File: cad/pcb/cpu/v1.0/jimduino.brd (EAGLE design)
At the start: 38 x 31 mm, 37 parts, among them P1 DF12-32-DP, P2 DF12-32-DP, Q1 FDN360P, SW1 ON/OFF, U1 STM32F415R, U2 MCP1703, U4 LTC2954-2, Y1 8Y-16.000MAAV-T, Y2 16MHz

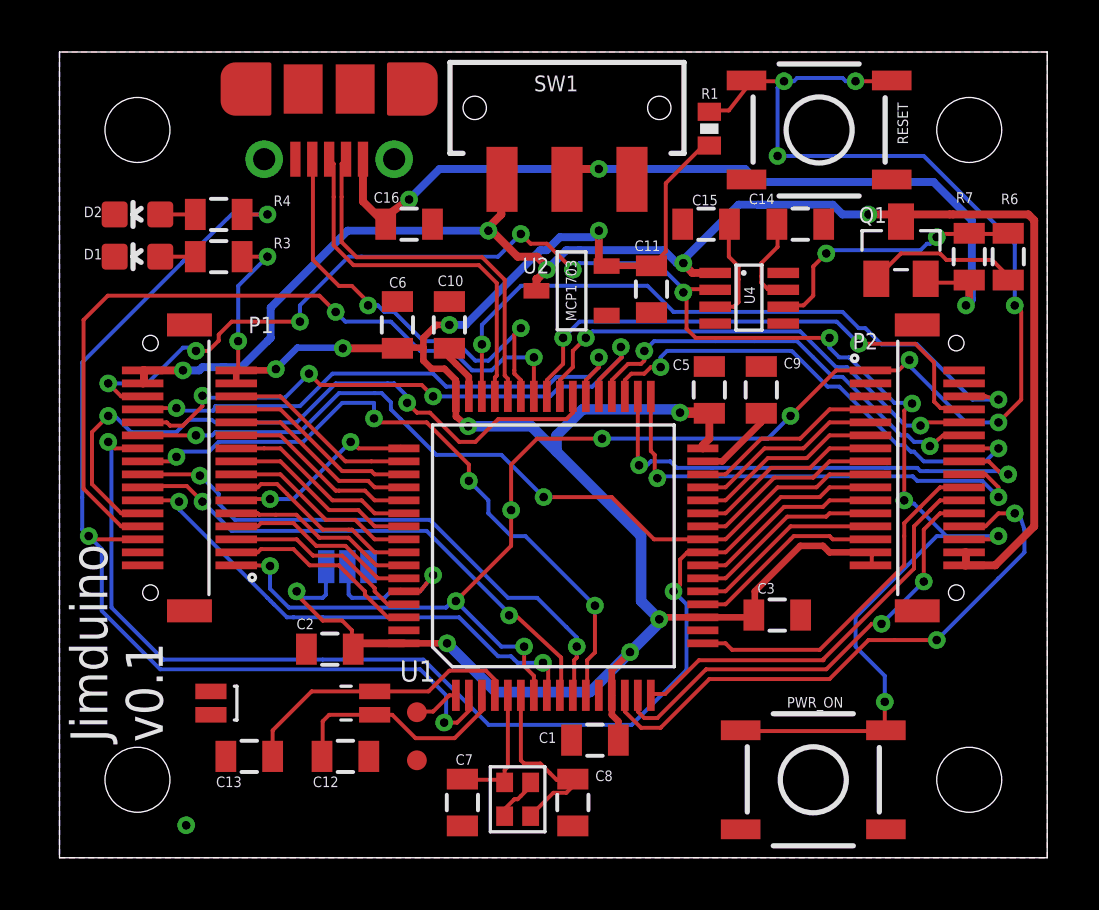
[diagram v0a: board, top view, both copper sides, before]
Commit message: Move components and switches around.
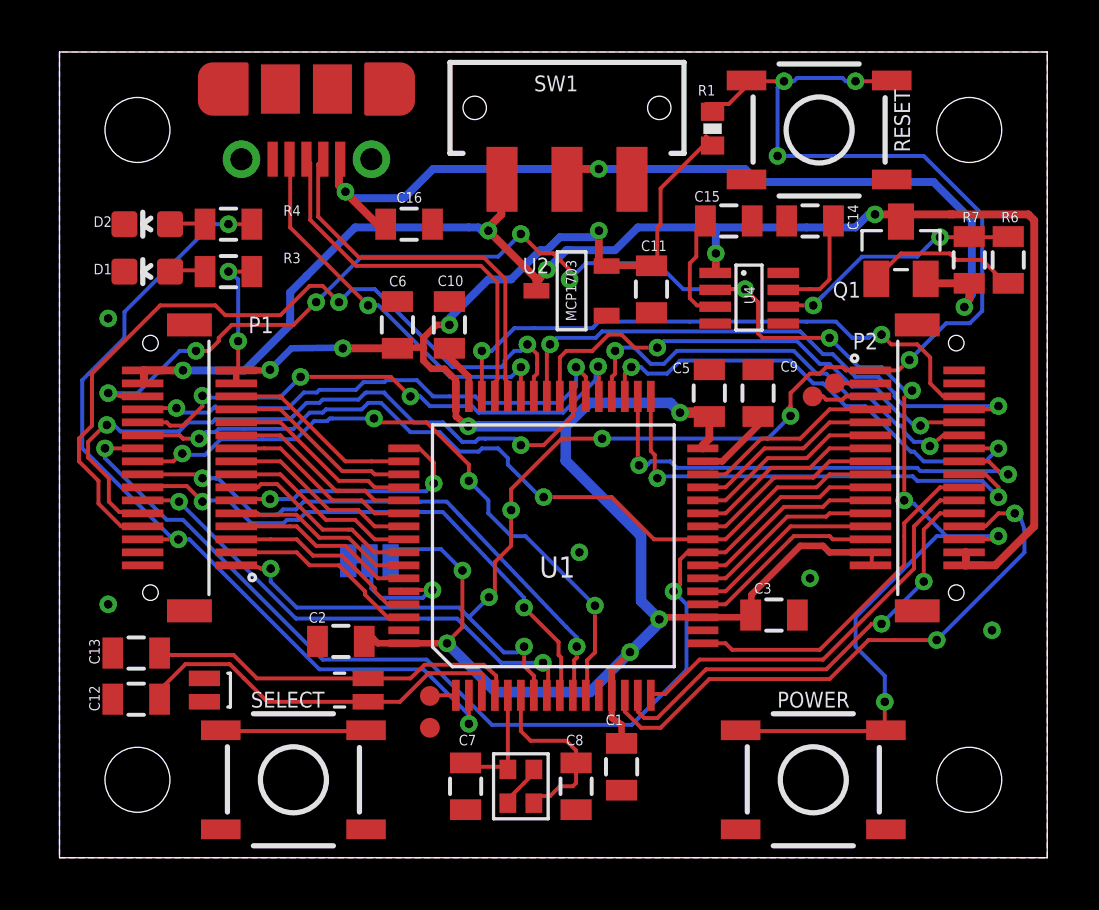
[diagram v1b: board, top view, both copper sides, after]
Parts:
- added SELECT: SWITCH-MOMENTARY-2SMD-REDUNDANT, SparkFun-Electromechanical:TACTILE-SWITCH-SMD
- added TP3, TP4: TEST-POINT3, SparkFun-Passives:PAD.03X.03
- C15: value 0.033uF -> .033uF
- moved C12 8.35 mm to (2.95, 6.10), turned to 180 degrees
- moved C13 5.89 mm to (2.95, 7.88)
- moved C1 1.45 mm to (21.6, 3.50), turned to 270 degrees
- moved TP2 1.35 mm to (14.2, 5.00)
- moved C15 0.88 mm to (25.8, 24.5), turned to 0 degrees
- moved BOOT0 0.88 mm to (11.9, 11.4), turned to 0 degrees
- moved U$3 0.88 mm to (12.0, 26.9)
- moved TP1 0.80 mm to (14.2, 6.22)
- moved D1 0.69 mm to (3.38, 22.6)
- moved R3 0.69 mm to (6.50, 22.6)
- moved C7 0.64 mm to (15.6, 2.75)
- moved C8 0.64 mm to (19.9, 2.75)
- moved Y2 0.56 mm to (12.5, 7.20)
- moved D2 0.53 mm to (3.38, 24.4)
- moved R4 0.53 mm to (6.50, 24.4)
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- renumbered PWR_ON to POWER
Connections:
- new net RSV0: P2.3, TP3.P$1
- new net RSV1: P2.5, TP4.P$1
- new net SELECT: SELECT.1, SELECT.2
- net GND: now also SELECT.3, SELECT.4
- net VCC_SW: no longer U4.1
- net VCC_USB: now also U4.1
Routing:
- net PC13: track 40.2 -> 34.3 mm
- net RESET#: track 74.8 -> 69.0 mm, vias 12 -> 10
- net SELECT: track 0.00 -> 5.61 mm
- net OSC32K_IN: track 10.0 -> 15.1 mm
- net PA13: track 26.5 -> 22.7 mm
- net PC4: track 45.8 -> 42.4 mm
- net OSC32K_OUT: track 11.3 -> 14.6 mm
- net PA14: track 7.60 -> 10.4 mm
- net RSV1: track 0.00 -> 2.33 mm
- net PC6: track 23.3 -> 21.5 mm
- net USB_ID: track 16.9 -> 15.2 mm
- net PA8: track 20.5 -> 22.1 mm
- net VCC_USB: track 36.5 -> 38.0 mm
- net BOOT0: track 6.52 -> 5.11 mm
- net RSV0: track 0.00 -> 1.37 mm
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
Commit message: Add LIPO charging circuit.
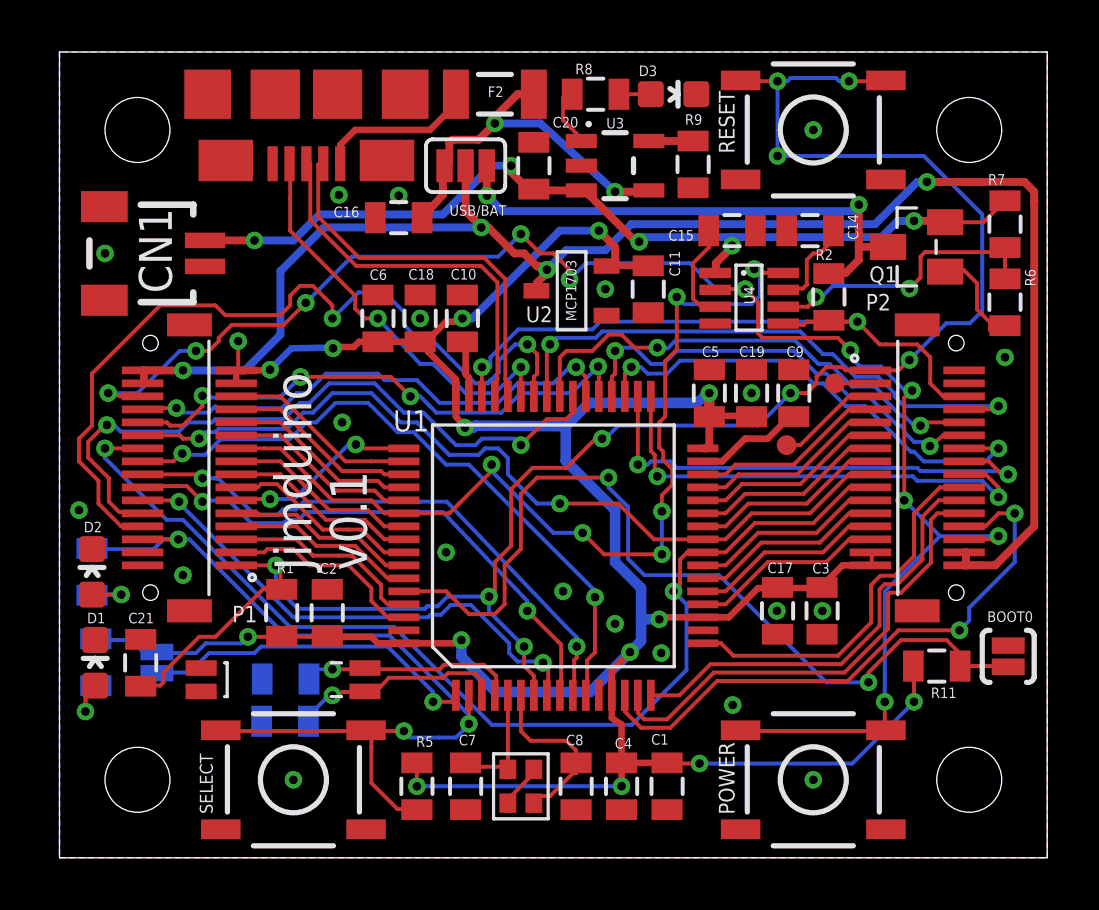
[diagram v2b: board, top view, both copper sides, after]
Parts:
- removed SW1: ON/OFF, SparkFun-Electromechanical:SWITCH-SPDT-SMD
- removed TP1, TP2: TEST-POINT3, SparkFun-Passives:PAD.03X.03
- removed U$3: USB-CON-5PIN-105017-0001, GeekAmmo:USB-MICRO-MOLEX-105017-0001
- added BKUP: JUMPER-PAD-2-NC_BY_PASTE, SparkFun-Passives:PAD-JUMPER-2-NC_BY_PASTE_YES_SILK
- added C17, C18, C21, C4: 0.1uF, SparkFun-Capacitors:0805
- added C19: 1uF, SparkFun-Capacitors:0805
- added C20: 10uF, SparkFun-Capacitors:0805
- added CN1: SM02B-SRSS-TB, con-jst2:SM02B-SRSS-TB
- added D3: CHG, SparkFun-LED:LED-0603
- added F2: PTCSMD, SparkFun-PowerIC:PTC-1206
- added P3: MICROUSB, jimduino:MICROUSB
- added R11, R2, R5: 10k, SparkFun-Passives:0805
- added R8: 1k, SparkFun-Passives:0805
- added R9: 4.7k, SparkFun-Passives:0805
- added U3: MCP73831, SparkFun-PowerIC:SOT23-5
- added USB/BAT: JUMPER-PAD-3-2OF3_NC_BY_PASTE, SparkFun-Passives:PAD-JUMPER-3-2OF3_NC_BY_PASTE_YES_SILK_FULL_BOX
- BOOT0: value JUMPER-PAD-3-2OF3_NC_BY_PASTE -> JUMPER-PAD-2-NC_BY_PASTE; device SparkFun-Passives:PAD-JUMPER-3-2OF3_NC_BY_PASTE_YES_SILK_FULL_BOX -> SparkFun-Passives:PAD-JUMPER-2-NC_BY_PASTE_YES_SILK
- C5: value 1uF -> 0.1uF
- D1: value RED_PWR -> PWR
- D2: value GREEN_PC13 -> PC13
- R1: device SparkFun-Passives:0402-RES -> SparkFun-Passives:0805
- R3, R4: value 270 -> 1k
- Y2: value 16MHz -> 32.768kHz
- moved R1 24.9 mm to (8.55, 9.43)
- moved BOOT0 24.8 mm to (36.5, 7.75), flipped to the top, turned to 90 degrees
- moved R3 15.9 mm to (1.40, 7.53), flipped to the bottom, turned to 90 degrees
- moved D1 15.2 mm to (1.38, 7.50), turned to 0 degrees
- moved R4 14.4 mm to (1.25, 11.0), flipped to the bottom, turned to 90 degrees
- moved D2 13.5 mm to (1.25, 11.0), turned to 0 degrees
- moved C13 5.84 mm to (8.70, 6.88), flipped to the bottom, turned to 0 degrees
- moved C12 5.79 mm to (8.68, 5.25), flipped to the bottom, turned to 0 degrees
- moved TP4 2.12 mm to (28.0, 15.9)
- moved R7 1.94 mm to (36.4, 24.4), turned to 270 degrees
- moved C1 1.90 mm to (23.4, 2.75)
- moved C3 1.86 mm to (29.3, 9.50), turned to 270 degrees
- moved R6 1.63 mm to (36.4, 21.4)
- moved C9 1.38 mm to (28.2, 17.9)
- moved C2 1.22 mm to (10.3, 9.43), turned to 90 degrees
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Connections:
- removed net INT#: U4.5
- removed net KILL#: U4.8
- removed net SELECT: SELECT.1, SELECT.2
- removed net USB_ID: U$3.4, U1.43
- removed net USB_N: U$3.2, U1.44
- removed net USB_P: U$3.3, U1.45
- removed net VCC_SW: P1.30, P1.32, P2.30, P2.32, Q1.3, SW1.1, U2.3
- new net N$10: D3.A, R8.1
- new net N$11: R9.1, U3.5
- new net PA10: P3.P$4, U1.43
- new net PA11: P3.P$2, U1.44
- new net PA12: P3.P$3, U1.45
- new net STAT: R8.2, U3.1
- new net VCC: P1.30, P1.32, P2.30, P2.32, U2.3, USB/BAT.2
- new net VCC_BKUP: BKUP.1, U1.1
- new net VCC_SOFT: Q1.3, R2.1, USB/BAT.1
- new net VCC_USB_FUSED: C16.1, F2.2, U3.4, USB/BAT.3
- net BOOT0: now also BOOT0.1, R11.1; no longer BOOT0.2
- net GND: now also BOOT0.2, C17.2, C18.2, C19.2, C20.2, C21.2, C4.2, CN1.2, D3.C, P3.P$5, R9.2, U3.2; no longer BOOT0.3, TP2.P$1, U$3.5
- net PA13: now also R2.2, U4.5
- net PC13: now also R5.1, SELECT.1, SELECT.2
- net PD2: now also U4.8
- net RESET#: now also C21.1
- net VBAT: now also C20.1, CN1.1, Q1.2, R7.1, U3.3, U4.1; no longer TP1.P$1, U1.1
- net VCC_3V3: now also BKUP.2, C17.1, C18.1, C19.1, C4.1, R11.2, R5.2; no longer BOOT0.1
- net VCC_USB: now also F2.1, P3.P$1; no longer C16.1, Q1.2, R7.1, SW1.2, U$3.1, U4.1
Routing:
- net VCC: track 0.00 -> 61.8 mm, vias 0 -> 4
- net VCC_SW: track 60.6 -> 0.00 mm, vias 5 -> 0
- net VBAT: track 1.00 -> 36.5 mm, vias 0 -> 5
- net VCC_USB: track 38.0 -> 6.63 mm, vias 3 -> 0
- net BOOT0: track 5.11 -> 34.6 mm, vias 1 -> 2
- net PD2: track 7.49 -> 36.6 mm, vias 0 -> 6
- net VCC_3V3: track 92.4 -> 113.3 mm, vias 12 -> 15
- net VCC_SOFT: track 0.00 -> 20.4 mm, vias 0 -> 2
- net PA10: track 0.00 -> 16.5 mm, vias 0 -> 2
- net USB_ID: track 15.2 -> 0.00 mm, vias 2 -> 0
- net USB_N: track 15.0 -> 0.00 mm
- net USB_P: track 15.0 -> 0.00 mm
- net PA12: track 0.00 -> 15.0 mm
- net PA11: track 0.00 -> 15.0 mm
- net VCC_USB_FUSED: track 0.00 -> 14.4 mm, vias 0 -> 2
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
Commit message: Add more intelligent power switching and improve schematic layout.
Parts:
- removed F2: PTCSMD, SparkFun-PowerIC:PTC-1206
- removed TP4: TEST-POINT3, SparkFun-Passives:PAD.03X.03
- removed USB/BAT: JUMPER-PAD-3-2OF3_NC_BY_PASTE, SparkFun-Passives:PAD-JUMPER-3-2OF3_NC_BY_PASTE_YES_SILK_FULL_BOX
- added D5: MBR120, SparkFun-DiscreteSemi:SOD-123
- added F1: PTCSMD, SparkFun-PowerIC:PTC-1206
- added Q2: FDN360P, transistor-power:SUPER-SOT3
- added R10: 100k, SparkFun-Passives:0805
- added R12: 10k, SparkFun-Passives:0805
- added RSV1, RSV2, RSV3: TEST-POINT3, SparkFun-Passives:PAD.03X.03
- moved D3 7.06 mm to (17.1, 26.6), turned to 180 degrees
- moved C20 3.12 mm to (16.4, 24.1), turned to 180 degrees
- moved R8 2.48 mm to (19.4, 27.2), turned to 0 degrees
- moved U3 2.15 mm to (20.1, 24.9)
- moved R9 2.11 mm to (23.0, 25.1)
- moved R6 0.62 mm to (36.4, 20.8)
- moved R7 0.62 mm to (36.4, 23.8)
- moved P3 0.53 mm to (10.0, 29.6)
- moved C16 0.50 mm to (13.1, 24.1)
- moved Q1 0.50 mm to (33.5, 23.5)
- moved C14 0.28 mm to (29.1, 24.0)
- moved C11 0.25 mm to (22.6, 21.6)
- moved R2 0.25 mm to (29.9, 21.6)
- moved U4 0.25 mm to (25.5, 22.5)
- moved C15 0.12 mm to (25.9, 24.0)
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- renumbered SELECT to SW1, TP3 to RSV0
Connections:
- removed net VCC_SOFT: Q1.3, R2.1, USB/BAT.1
- removed net VCC_USB_FUSED: C16.1, F2.2, U3.4, USB/BAT.3
- new net RSV2: P2.17, RSV2.P$1
- new net RSV3: P2.19, RSV3.P$1
- new net VCC_SEL: D5.C, Q1.2, Q2.2, R7.1, U4.1
- new net VCC_USBF: C16.1, D5.A, F1.2, Q2.1, R10.1, U3.4
- net GND: now also P3.10, P3.11, P3.5, P3.6, P3.7, P3.8, P3.9, R10.2; no longer P3.P$5
- net PA10: now also P3.4; no longer P3.P$4
- net PA11: now also P3.2; no longer P3.P$2
- net PA12: now also P3.3; no longer P3.P$3
- net PC4: no longer P2.19
- net PC5: no longer P2.17
- net PD2: now also R12.2
- net RSV1: now also RSV1.P$1; no longer TP4.P$1
- net VBAT: now also Q2.3; no longer Q1.2, R7.1, U4.1
- net VCC: now also Q1.3; no longer USB/BAT.2
- net VCC_3V3: now also R12.1, R2.1
- net VCC_USB: now also F1.1, P3.1; no longer F2.1, P3.P$1
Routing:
- net PD2: track 36.6 -> 70.3 mm, vias 6 -> 8
- net VCC_SEL: track 0.00 -> 26.0 mm, vias 0 -> 4
- net VCC_USBF: track 0.00 -> 20.9 mm, vias 0 -> 5
- net VCC_SOFT: track 20.4 -> 0.00 mm, vias 2 -> 0
- net VCC_USB_FUSED: track 14.4 -> 0.00 mm, vias 2 -> 0
- net VCC_3V3: track 113.3 -> 126.0 mm, vias 15 -> 18
- net VBAT: track 36.5 -> 28.5 mm, vias 5 -> 3
- net PC5: track 32.7 -> 25.2 mm
- net PC4: track 42.4 -> 34.9 mm
- net RSV2: track 0.00 -> 4.75 mm
- net RSV3: track 0.00 -> 2.92 mm
- net VCC_USB: track 6.63 -> 9.40 mm, vias 0 -> 2
- net VCC: track 61.8 -> 59.3 mm, vias 4 -> 3
- net RSV1: track 4.00 -> 1.93 mm
- net N$8: track 11.3 -> 12.8 mm
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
